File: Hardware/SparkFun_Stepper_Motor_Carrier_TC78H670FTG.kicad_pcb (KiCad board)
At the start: 4 copper layers, 15.2 x 20.3 mm, 42 parts, among them J1 Conn_01x08, J2 Conn_01x08, U1 TC78H670FTG

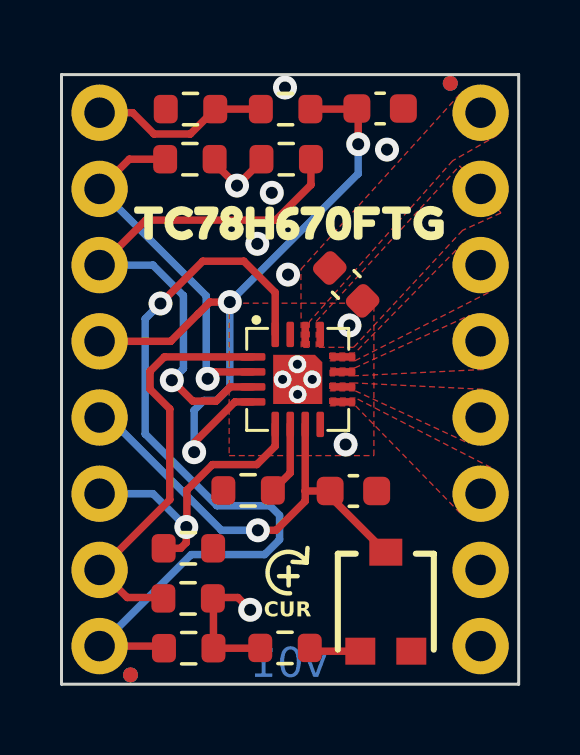
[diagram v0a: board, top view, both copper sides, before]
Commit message: more stuff pre-review
-copper weight added to ordering instructions
-removed old sym library from project table (eagle import from older prodriver)
-added CC license to sch
-added M2 and M3 to buzzard labels for STEP and DIR
-copper edge clearance in DRC set to 0.2mm
-excluded DRC errors that I wish to ignore
-used one signle GND zone for top in1 and bottom copper ground pours
-adjusted clearances/min-widths/spoke-thickness/DRC to get ideal GND zone flow.
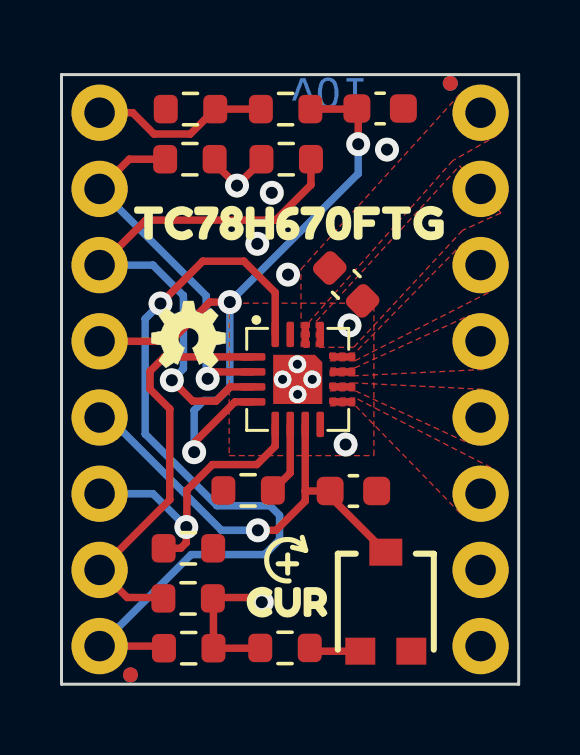
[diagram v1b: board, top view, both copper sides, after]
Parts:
- removed kibuzzard-65CFAD5D: G***, kibuzzard-65CFAD5D
- removed kibuzzard-65CFAD73: G***, kibuzzard-65CFAD73
- added kibuzzard-65D52B03: G***, kibuzzard-65D52B03, B.Cu at (140.1, 110.5)
- added kibuzzard-65D52B32: G***, kibuzzard-65D52B32, B.Cu at (139.4, 113.0)
- added kibuzzard-65D531EE: G***, kibuzzard-65D531EE, F.Cu at (142.1, 111.6)
- added ref**1: val**, SparkFun-Aesthetic:Creative_Commons_License, F.Cu at (139.7, 137.2)
- Ref**: moved to F.Cu
- moved Ref** 9.82 mm to (138.9, 102.8), turned to 0 degrees
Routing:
- net GND: vias 11 -> 10
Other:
- board text added: "Copper weight: 2oz"
- board text removed: "CUR"

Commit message: add sfe flame logo
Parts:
- added REF**: SFE_FLAME_0.1, SparkFun-Aesthetic:SFE_FLAME_0.1, F.Cu at (146.1, 102.7)
